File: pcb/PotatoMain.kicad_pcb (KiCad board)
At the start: 2 copper layers, 53.4 x 55.2 mm, 26 parts, among them P1 CONN_01X03, P2 CONN_01X03, P3 CONN_01X02, U1 arduino_mini

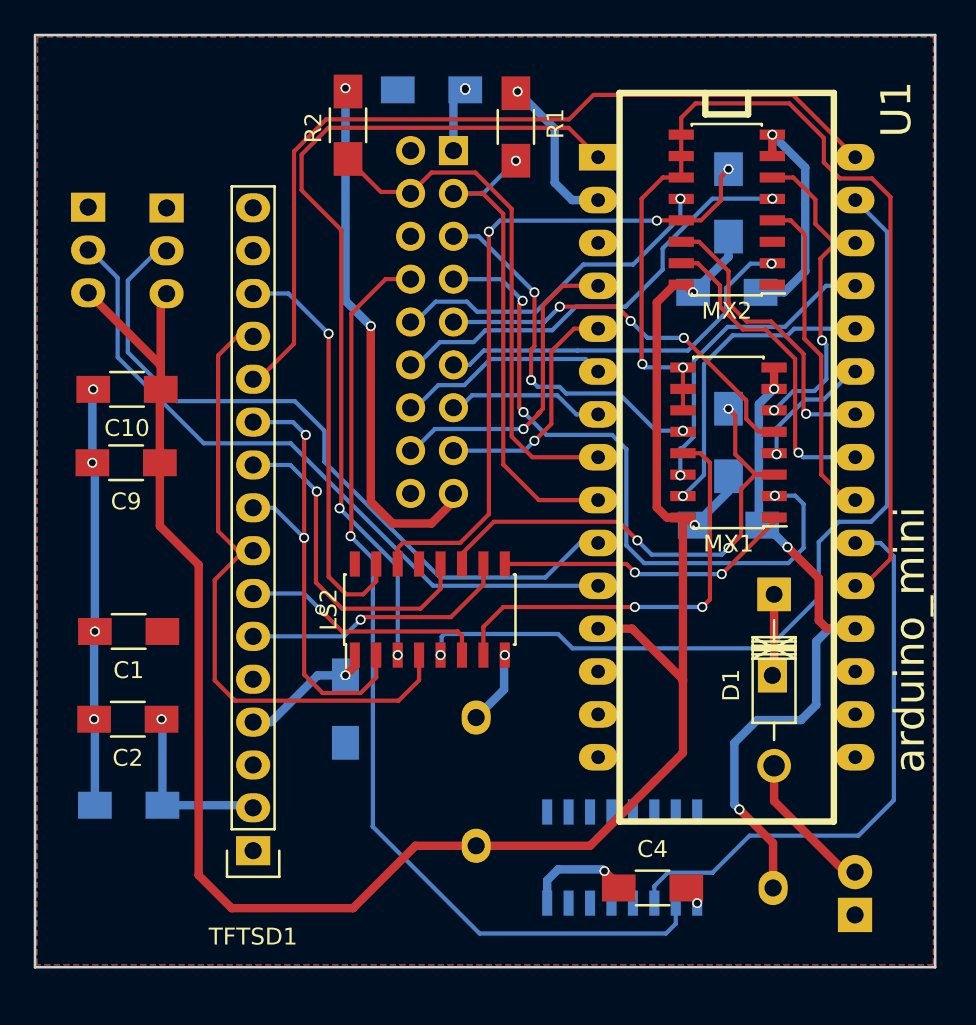
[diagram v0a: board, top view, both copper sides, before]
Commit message: made PCB smaller
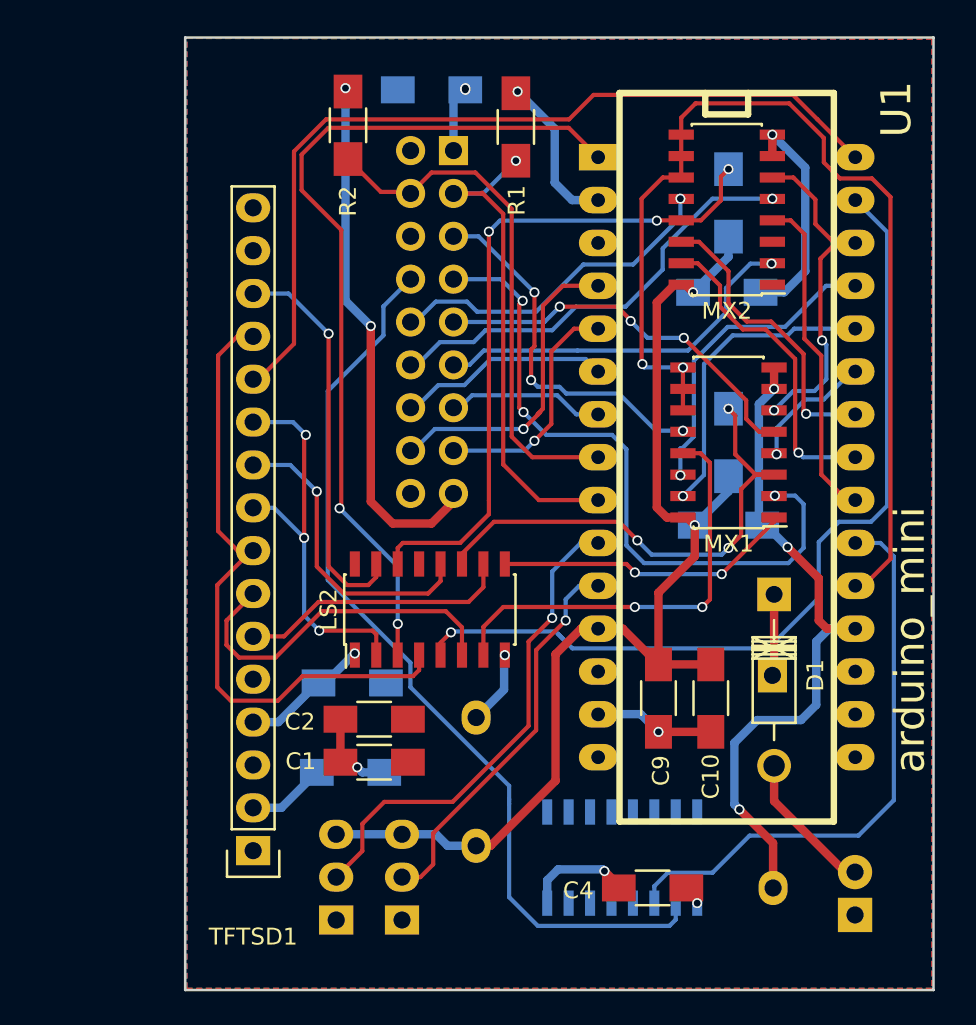
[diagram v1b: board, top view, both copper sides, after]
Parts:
- moved P2 46.2 mm to (114.5, 108.3), turned to 0 degrees
- moved P1 43.4 mm to (110.7, 108.3), turned to 0 degrees
- moved C10 39.1 mm to (132.8, 95.2), turned to 270 degrees
- moved C9 34.5 mm to (129.8, 95.2), turned to 270 degrees
- moved C1 16.5 mm to (112.9, 99.0)
- moved C2 14.6 mm to (112.9, 96.4)
- moved C7 13.3 mm to (111.5, 99.5), turned to 0 degrees
- moved C6 1.60 mm to (111.6, 94.2), turned to 0 degrees
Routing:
- net +5V: track 120.9 -> 67.7 mm
- net Net-(P2-Pad2): track 41.1 -> 23.4 mm, vias 0 -> 1
- net Net-(P1-Pad2): track 42.8 -> 30.3 mm, vias 0 -> 1
- net GND: track 90.0 -> 77.7 mm, vias 10 -> 8
- net Net-(LS2-Pad6): track 14.6 -> 21.1 mm, vias 1 -> 0
- net +3V3: track 65.2 -> 59.2 mm, vias 8 -> 7
- net Net-(LS2-Pad2): track 27.9 -> 23.9 mm, vias 2 -> 3
- net Net-(LS1-Pad2): track 57.4 -> 54.8 mm, vias 1 -> 0
- net Net-(LS2-Pad12): track 19.8 -> 18.3 mm
- net Net-(LS2-Pad15): track 24.5 -> 23.5 mm
- net Net-(LS2-Pad5): track 52.3 -> 52.8 mm
- net Net-(LS2-Pad10): track 16.1 -> 16.2 mm, vias 1 -> 0
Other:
- board size 53.4 x 55.2 mm -> 44.4 x 56.5 mm
